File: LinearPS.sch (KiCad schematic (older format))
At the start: 102 parts, among them J1 Conn_01x03, J10 Conn_01x01, J11 Conn_01x01, J12 Conn_01x01, J14 Conn_01x01, J2 Conn_01x02, J3 Conn_01x03, J4 Conn_01x01, J5 Conn_01x01, J6 Conn_01x01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

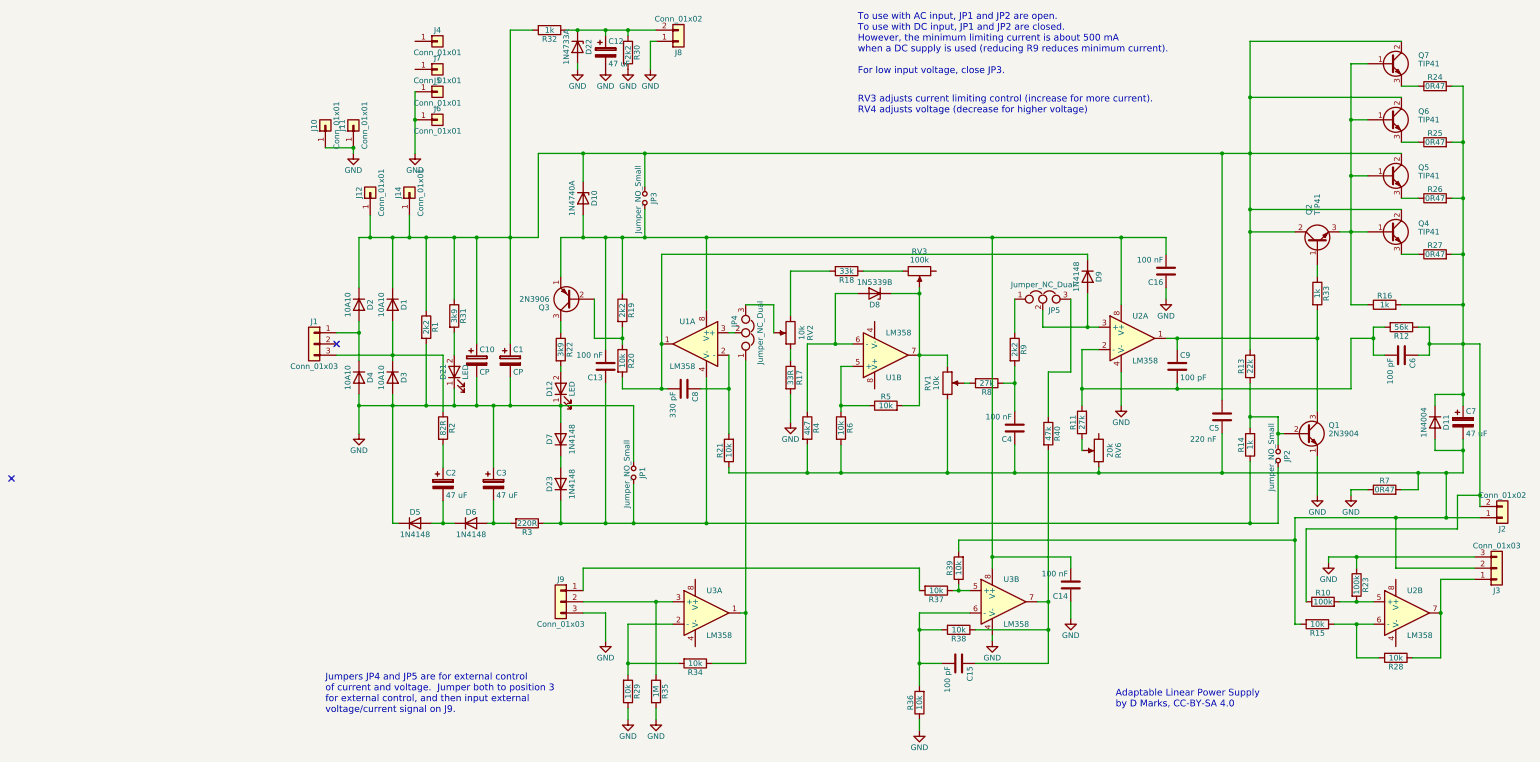
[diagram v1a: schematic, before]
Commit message: Added extra pin to get reference voltage
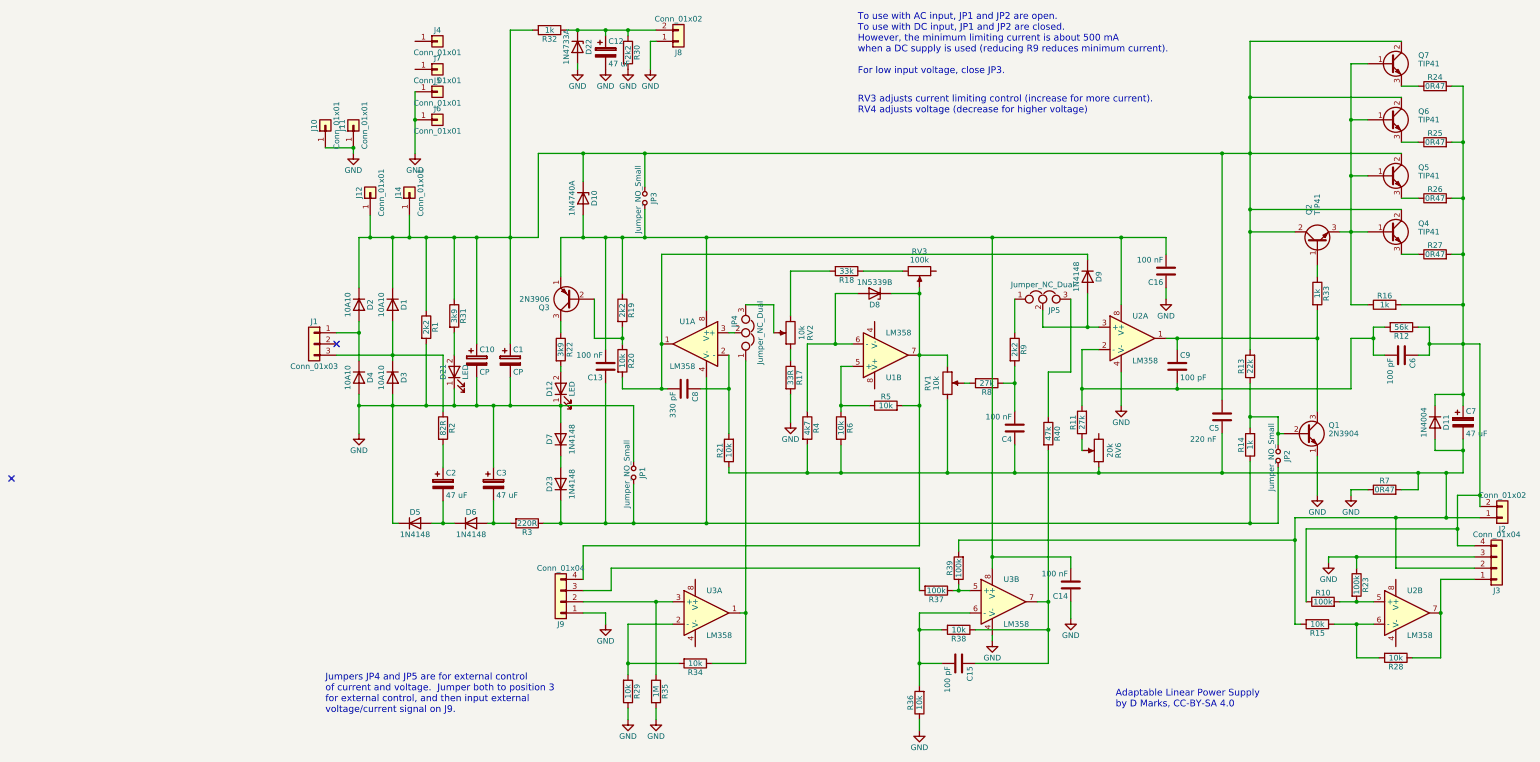
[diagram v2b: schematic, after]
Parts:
- removed J3, J9: Conn_01x03, Connectors_Molex:Molex_KK-6410-03_03x2.54mm_Straight, symbol Conn_01x03
- added J3, J9: Conn_01x04, Connectors_Molex:Molex_KK-6410-04_04x2.54mm_Straight, symbol Conn_01x04
- R37, R39: value 10k -> 100k
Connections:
- net GND: now also J3.3 (Pin_3), J9.1 (Pin_1)
- net at C4.1, C5.1, C7.2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: now also J3.2 (Pin_2)
- net at C6.1, C7.1, D11.1 (K)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: now also J3.4 (Pin_4)
- net at D8.1 (K), R5.2, RV1.1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: now also J9.4 (Pin_4)
- net at R28.1, U2.7: now also J3.1 (Pin_1)
- net at R35.1, U3.3 (+): now also J9.2 (Pin_2)
- net at R37.2: now also J9.3 (Pin_3)
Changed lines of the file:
@@
 $EndComp
 $Comp
-L GND #PWR2
+L GND #PWR01
 U 1 1 5CEC838A
 P 950 4450
-F 0 "#PWR2" H 950 4200 50  0001 C CNN
+F 0 "#PWR01" H 950 4200 50  0001 C CNN
 F 1 "GND" H 950 4300 50  0000 C CNN
 F 2 "" H 950 4450 50  0001 C CNN
@@
 $EndComp
 $Comp
-L Conn_01x03 J3
-U 1 1 5CEFCEB0
-P 11100 5650
-F 0 "J3" H 11100 5850 50  0000 C CNN
-F 1 "Conn_01x03" H 11100 5450 50  0000 C CNN
-F 2 "Connectors_Molex:Molex_KK-6410-03_03x2.54mm_Straight" H 11100 5650 50  0001 C CNN
-F 3 "" H 11100 5650 50  0001 C CNN
-	1    11100 5650
-	1    0    0    1
-$EndComp
-$Comp
 L R R24
 U 1 1 5CEFEB2A
@@
 $EndComp
 $Comp
-L GND #PWR4
+L GND #PWR02
 U 1 1 5CECFA19
 P 2900 1200
-F 0 "#PWR4" H 2900 950 50  0001 C CNN
+F 0 "#PWR02" H 2900 950 50  0001 C CNN
 F 1 "GND" H 2900 1050 50  0000 C CNN
 F 2 "" H 2900 1200 50  0001 C CNN
@@
 $EndComp
 $Comp
-L GND #PWR9
+L GND #PWR03
 U 1 1 5CED04A2
 P 3550 1200
-F 0 "#PWR9" H 3550 950 50  0001 C CNN
+F 0 "#PWR03" H 3550 950 50  0001 C CNN
 F 1 "GND" H 3550 1050 50  0000 C CNN
 F 2 "" H 3550 1200 50  0001 C CNN
@@
 $EndComp
 $Comp
-L GND #PWR5
+L GND #PWR04
 U 1 1 5CED0ACE
 P 3150 1200
-F 0 "#PWR5" H 3150 950 50  0001 C CNN
+F 0 "#PWR04" H 3150 950 50  0001 C CNN
 F 1 "GND" H 3150 1050 50  0000 C CNN
 F 2 "" H 3150 1200 50  0001 C CNN
@@
 $EndComp
 $Comp
-L GND #PWR7
+L GND #PWR05
 U 1 1 5CED1C83
 P 3350 1200
-F 0 "#PWR7" H 3350 950 50  0001 C CNN
+F 0 "#PWR05" H 3350 950 50  0001 C CNN
 F 1 "GND" H 3350 1050 50  0000 C CNN
 F 2 "" H 3350 1200 50  0001 C CNN
@@
 $EndComp
 $Comp
-L Conn_01x03 J9
-U 1 1 5D2A116B
-P 2750 5950
-F 0 "J9" H 2750 6150 50  0000 C CNN
-F 1 "Conn_01x03" H 2750 5750 50  0000 C CNN
-F 2 "Connectors_Molex:Molex_KK-6410-03_03x2.54mm_Straight" H 2750 5950 50  0001 C CNN
-F 3 "" H 2750 5950 50  0001 C CNN
-	1    2750 5950
-	-1   0    0    -1
-$EndComp
-$Comp
 L R R37
 U 1 1 5D2A21C5
 P 6100 5850
 F 0 "R37" V 6180 5850 50  0000 C CNN
-F 1 "10k" V 6100 5850 50  0000 C CNN
+F 1 "100k" V 6100 5850 50  0000 C CNN
 F 2 "Resistors_THT:R_Axial_DIN0207_L6.3mm_D2.5mm_P7.62mm_Horizontal" V 6030 5850 50  0001 C CNN
 F 3 "" H 6100 5850 50  0001 C CNN
@@
 $EndComp
 $Comp
-L GND #PWR13
+L GND #PWR06
 U 1 1 5D2A363C
 P 6600 6300
-F 0 "#PWR13" H 6600 6050 50  0001 C CNN
+F 0 "#PWR06" H 6600 6050 50  0001 C CNN
 F 1 "GND" H 6600 6150 50  0000 C CNN
 F 2 "" H 6600 6300 50  0001 C CNN
@@
 $EndComp
 $Comp
-L GND #PWR12
-U 1 1 5D2A4408
-P 5950 7100
-F 0 "#PWR12" H 5950 6850 50  0001 C CNN
-F 1 "GND" H 5950 6950 50  0000 C CNN
-F 2 "" H 5950 7100 50  0001 C CNN
-F 3 "" H 5950 7100 50  0001 C CNN
-	1    5950 7100
-	1    0    0    -1
-$EndComp
-$Comp
-L R R39
-U 1 1 5D2A4BCC
-P 6300 5650
-F 0 "R39" V 6380 5650 50  0000 C CNN
-F 1 "10k" V 6300 5650 50  0000 C CNN
-F 2 "Resistors_THT:R_Axial_DIN0207_L6.3mm_D2.5mm_P7.62mm_Horizontal" V 6230 5650 50  0001 C CNN
-F 3 "" H 6300 5650 50  0001 C CNN
-	1    6300 5650
-	-1   0    0    1
-$EndComp
-$Comp
-L GND #PWR6
-U 1 1 5D2A5B2D
-P 3150 6300
-F 0 "#PWR6" H 3150 6050 50  0001 C CNN
-F 1 "GND" H 3150 6150 50  0000 C CNN
-F 2 "" H 3150 6300 50  0001 C CNN
-F 3 "" H 3150 6300 50  0001 C CNN
-	1    3150 6300
-	1    0    0    -1
-$EndComp
-$Comp
 L C C14
 U 1 1 5D2A7781
@@
 $EndComp
 $Comp
-L GND #PWR14
+L GND #PWR07
 U 1 1 5D2A7B6A
 P 7300 6100
-F 0 "#PWR14" H 7300 5850 50  0001 C CNN
+F 0 "#PWR07" H 7300 5850 50  0001 C CNN
 F 1 "GND" H 7300 5950 50  0000 C CNN
 F 2 "" H 7300 6100 50  0001 C CNN
@@
 	0    1    -1   0
 $EndComp
-Text Notes 650  6950 0    60   ~ 0
-Jumpers JP4 and JP5 are for external control\nof current and voltage.  Jumper both to position 3\nfor external control, and then input external\nvoltage/current signal on J9.
 $Comp
 L R R40
@@
 F 3 "" H 7100 4450 50  0001 C CNN
 	1    7100 4450
-	1    0    0    -1
-$EndComp
-$Comp
-L GND #PWR8
-U 1 1 5D2A7293
-P 3350 7000
-F 0 "#PWR8" H 3350 6750 50  0001 C CNN
-F 1 "GND" H 3350 6850 50  0000 C CNN
-F 2 "" H 3350 7000 50  0001 C CNN
-F 3 "" H 3350 7000 50  0001 C CNN
-	1    3350 7000
 	1    0    0    -1
 $EndComp
@@
 $EndComp
 $Comp
-L GND #PWR3
+L GND #PWR08
 U 1 1 5D2BE3B3
 P 1450 1950
-F 0 "#PWR3" H 1450 1700 50  0001 C CNN
+F 0 "#PWR08" H 1450 1700 50  0001 C CNN
 F 1 "GND" H 1450 1800 50  0000 C CNN
 F 2 "" H 1450 1950 50  0001 C CNN
@@
 $EndComp
 $Comp
-L GND #PWR16
+L GND #PWR09
 U 1 1 5D5FCB6F
 P 8150 3250
-F 0 "#PWR16" H 8150 3000 50  0001 C CNN
+F 0 "#PWR09" H 8150 3000 50  0001 C CNN
 F 1 "GND" H 8150 3100 50  0000 C CNN
 F 2 "" H 8150 3250 50  0001 C CNN
@@
 $EndComp
 $Comp
-L GND #PWR18
+L GND #PWR010
 U 1 1 5D5FFE57
 P 9600 5600
-F 0 "#PWR18" H 9600 5350 50  0001 C CNN
+F 0 "#PWR010" H 9600 5350 50  0001 C CNN
 F 1 "GND" H 9600 5450 50  0000 C CNN
 F 2 "" H 9600 5600 50  0001 C CNN
@@
 $EndComp
 $Comp
-L GND #PWR11
+L GND #PWR011
 U 1 1 5D606C21
 P 4800 4350
-F 0 "#PWR11" H 4800 4100 50  0001 C CNN
+F 0 "#PWR011" H 4800 4100 50  0001 C CNN
 F 1 "GND" H 4800 4200 50  0000 C CNN
 F 2 "" H 4800 4350 50  0001 C CNN
@@
 $EndComp
 $Comp
-L GND #PWR15
+L GND #PWR012
 U 1 1 5D608020
 P 7750 4200
-F 0 "#PWR15" H 7750 3950 50  0001 C CNN
+F 0 "#PWR012" H 7750 3950 50  0001 C CNN
 F 1 "GND" H 7750 4050 50  0000 C CNN
 F 2 "" H 7750 4200 50  0001 C CNN
@@
 $EndComp
 $Comp
-L GND #PWR17
+L GND #PWR013
 U 1 1 5D608830
 P 9500 5000
-F 0 "#PWR17" H 9500 4750 50  0001 C CNN
+F 0 "#PWR013" H 9500 4750 50  0001 C CNN
 F 1 "GND" H 9500 4850 50  0000 C CNN
 F 2 "" H 9500 5000 50  0001 C CNN
@@
 $EndComp
 $Comp
-L GND #PWR19
+L GND #PWR014
 U 1 1 5D60C78D
 P 9800 5000
-F 0 "#PWR19" H 9800 4750 50  0001 C CNN
+F 0 "#PWR014" H 9800 4750 50  0001 C CNN
 F 1 "GND" H 9800 4850 50  0000 C CNN
 F 2 "" H 9800 5000 50  0001 C CNN
@@
 $EndComp
 $Comp
-L GND #PWR1
+L GND #PWR015
 U 1 1 5D664C72
 P 900 1950
-F 0 "#PWR1" H 900 1700 50  0001 C CNN
+F 0 "#PWR015" H 900 1700 50  0001 C CNN
 F 1 "GND" H 900 1800 50  0000 C CNN
 F 2 "" H 900 1950 50  0001 C CNN
@@
 	2950 5950 3750 5950
 Wire Wire Line
-	2950 5650 5950 5650
-Wire Wire Line
-	2950 5850 2950 5650
+	3200 5650 5950 5650
 Wire Wire Line
 	7300 3250 7300 3900
@@
 	6600 5550 7300 5550
 Wire Wire Line
-	3350 7000 3350 6900
-Wire Wire Line
 	3350 6150 3750 6150
 Wire Wire Line
@@
 Wire Wire Line
 	3150 6050 2950 6050
-Wire Wire Line
-	3150 6050 3150 6300
 Connection ~ 3500 2700
 Wire Wire Line
@@
 	5700 3200 5950 3200
 Wire Wire Line
-	5950 3150 5950 4200
+	5950 3150 5950 5450
 Wire Wire Line
 	4800 3000 5150 3000
@@
 Wire Wire Line
 	2300 4200 2300 3950
-Wire Wire Line
-	2300 850  2300 3650
 Wire Wire Line
 	1700 3750 1700 4250
@@
 Connection ~ 2300 2700
 Wire Wire Line
-	2300 850  2500 850
-Wire Wire Line
 	3550 1200 3550 950
 Wire Wire Line
@@
 	9800 4950 9950 4950
 Wire Wire Line
-	10750 5300 10750 5000
+	10750 5000 10750 5450
 Wire Wire Line
 	10400 4950 10400 4800
@@
 $EndComp
 $Comp
-L GND #PWR10
+L GND #PWR016
 U 1 1 5D6D40A8
 P 3600 7000
-F 0 "#PWR10" H 3600 6750 50  0001 C CNN
+F 0 "#PWR016" H 3600 6750 50  0001 C CNN
 F 1 "GND" H 3600 6850 50  0000 C CNN
 F 2 "" H 3600 7000 50  0001 C CNN
@@
 	3600 6600 3600 5950
 Connection ~ 3600 5950
+Text Notes 650  6950 0    60   ~ 0
+Jumpers JP4 and JP5 are for external control\nof current and voltage.  Jumper both to position 3\nfor external control, and then input external\nvoltage/current signal on J9.
+$Comp
+L GND #PWR017
+U 1 1 5D2A4408
+P 5950 7100
+F 0 "#PWR017" H 5950 6850 50  0001 C CNN
+F 1 "GND" H 5950 6950 50  0000 C CNN
+F 2 "" H 5950 7100 50  0001 C CNN
+F 3 "" H 5950 7100 50  0001 C CNN
+	1    5950 7100
+	1    0    0    -1
+$EndComp
+$Comp
+L R R39
+U 1 1 5D2A4BCC
+P 6300 5650
+F 0 "R39" V 6380 5650 50  0000 C CNN
+F 1 "100k" V 6300 5650 50  0000 C CNN
+F 2 "Resistors_THT:R_Axial_DIN0207_L6.3mm_D2.5mm_P7.62mm_Horizontal" V 6230 5650 50  0001 C CNN
+F 3 "" H 6300 5650 50  0001 C CNN
+	1    6300 5650
+	-1   0    0    1
+$EndComp
+$Comp
+L GND #PWR018
+U 1 1 5D8338D4
+P 3150 6150
+F 0 "#PWR018" H 3150 5900 50  0001 C CNN
+F 1 "GND" H 3150 6000 50  0000 C CNN
+F 2 "" H 3150 6150 50  0001 C CNN
+F 3 "" H 3150 6150 50  0001 C CNN
+	1    3150 6150
+	1    0    0    -1
+$EndComp
+Wire Wire Line
+	3150 6150 3150 6050
+$Comp
+L GND #PWR019
+U 1 1 5D834333
+P 3350 7000
+F 0 "#PWR019" H 3350 6750 50  0001 C CNN
+F 1 "GND" H 3350 6850 50  0000 C CNN
+F 2 "" H 3350 7000 50  0001 C CNN
+F 3 "" H 3350 7000 50  0001 C CNN
+	1    3350 7000
+	1    0    0    -1
+$EndComp
+Wire Wire Line
+	3350 7000 3350 6900
+$Comp
+L Conn_01x04 J9
+U 1 1 5D880B5F
+P 2750 5950
+F 0 "J9" H 2750 6150 50  0000 C CNN
+F 1 "Conn_01x04" H 2750 5650 50  0000 C CNN
+F 2 "Connectors_Molex:Molex_KK-6410-04_04x2.54mm_Straight" H 2750 5950 50  0001 C CNN
+F 3 "" H 2750 5950 50  0001 C CNN
+	1    2750 5950
+	-1   0    0    1
+$EndComp
+Wire Wire Line
+	2950 5850 3200 5850
+Wire Wire Line
+	3200 5850 3200 5650
+Wire Wire Line
+	2950 5750 2950 5450
+Wire Wire Line
+	2950 5450 5950 5450
+Connection ~ 5950 4200
+$Comp
+L Conn_01x04 J3
+U 1 1 5D882497
+P 11100 5650
+F 0 "J3" H 11100 5850 50  0000 C CNN
+F 1 "Conn_01x04" H 11100 5350 50  0000 C CNN
+F 2 "Connectors_Molex:Molex_KK-6410-04_04x2.54mm_Straight" H 11100 5650 50  0001 C CNN
+F 3 "" H 11100 5650 50  0001 C CNN
+	1    11100 5650
+	1    0    0    1
+$EndComp
+Wire Wire Line
+	2300 850  2500 850
+Wire Wire Line
+	2300 850  2300 3650
+Wire Wire Line
+	10750 5450 10900 5450
+Connection ~ 10750 5300
 $EndSCHEMATC

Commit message: Updated Schematic
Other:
- note added: "For up to 30 volts supply, LM358 is sufficient\nFor up to 40 volts supply, use TL35072P instead of LM358"
- note added: "Jumpers JP4 and JP5 are for programmable\nsupply inputs. Jumper both to position 3 \nfor external control of both voltage and\ncurrent , and then input external \nvoltage/current signal on J9."
- note removed: "Jumpers JP4 and JP5 are for external control\nof current and voltage. Jumper both to position 3\nfor external control, and then input external\nvoltage/current signal on J9."
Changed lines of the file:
@@
 Text Notes 5400 1250 0    60   ~ 0
 To use with AC input, JP1 and JP2 are open.\nTo use with DC input, JP1 and JP2 are closed. \nHowever, the minimum limiting current is about 500 mA\nwhen a DC supply is used (reducing R9 reduces minimum current).\n\nFor low input voltage, close JP3.
-Text Notes 5400 1600 0    60   ~ 0
+Text Notes 5400 1500 0    60   ~ 0
 RV3 adjusts current limiting control (increase for more current).\nRV4 adjusts voltage (decrease for higher voltage)
 $Comp
@@
 Connection ~ 3600 5950
 Text Notes 650  6950 0    60   ~ 0
-Jumpers JP4 and JP5 are for external control\nof current and voltage.  Jumper both to position 3\nfor external control, and then input external\nvoltage/current signal on J9.
+Jumpers JP4 and JP5 are for programmable\nsupply inputs.  Jumper both to position 3 \nfor external control of both voltage and\ncurrent , and then input external \nvoltage/current signal on J9.
 $Comp
 L GND #PWR017
@@
 	10750 5450 10900 5450
 Connection ~ 10750 5300
+Text Notes 5400 1750 0    60   ~ 0
+For up to 30 volts supply, LM358 is sufficient\nFor up to 40 volts supply, use TL35072P instead of LM358
 $EndSCHEMATC
